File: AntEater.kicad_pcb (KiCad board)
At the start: 2 copper layers, 50.1 x 30.1 mm, 5 parts, among them CN1 X2026WRS-2X09D-LPSW, CN2 X2026WRS-2X09D-LPSW, J1 Conn_01x10_MountingPin

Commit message: placed and routed
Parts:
- removed J1: Conn_01x10_MountingPin, Connector_PinHeader_2.54mm:PinHeader_1x11_P2.54mm_Vertical
- added C1: 0.1uF, Capacitor_SMD:C_0805_2012Metric, F.Cu at (161.4, 77.7)
- added C10: 3.3uF, Capacitor_SMD:C_0805_2012Metric, F.Cu at (161.1, 66.3)
- added C11: 0.1uF, Capacitor_SMD:C_0805_2012Metric, F.Cu at (176.4, 74.0)
- added C12: 0.1uF, Capacitor_SMD:C_0805_2012Metric, F.Cu at (165.3, 79.5)
- added C13: 0.1uF, Capacitor_SMD:C_0805_2012Metric, F.Cu at (161.1, 71.6)
- added C14: 0.1uF, Capacitor_SMD:C_0805_2012Metric, F.Cu at (161.1, 68.3)
- added C2: 27pf, Capacitor_SMD:C_0805_2012Metric, F.Cu at (154.8, 82.9)
- added C3: 0.1uF, Capacitor_SMD:C_0805_2012Metric, F.Cu at (176.0, 78.9)
- added C4: 4.7uF, Capacitor_SMD:C_1206_3216Metric, F.Cu at (164.7, 81.7)
- added C5: 0.1uF, Capacitor_SMD:C_0805_2012Metric, F.Cu at (175.4, 66.1)
- added C6: 4.7uF, Capacitor_SMD:C_1206_3216Metric, F.Cu at (171.4, 81.6)
- added C7: 27pf, Capacitor_SMD:C_0805_2012Metric, F.Cu at (161.1, 82.9)
- added C8: 0.1uF, Capacitor_SMD:C_0805_2012Metric, F.Cu at (177.3, 68.5)
- added C9: 0.1uF, Capacitor_SMD:C_0805_2012Metric, F.Cu at (170.3, 79.4)
- added FB1: FerriteBead_Small, Resistor_SMD:R_0603_1608Metric, F.Cu at (175.4, 81.4)
- added FB2: FerriteBead_Small, Resistor_SMD:R_0603_1608Metric, F.Cu at (175.4, 83.0)
- added J2: USB_C_Receptacle_USB2.0, Connector_USB:USB_C_Receptacle_GCT_USB4105-xx-A_16P_TopMnt_Horizontal, F.Cu at (168.4, 87.6)
- added J3: Conn_02x06_Odd_Even, Connector_PinHeader_2.54mm:PinHeader_2x06_P2.54mm_Vertical, F.Cu at (167.3, 46.2)
- added JP1: SolderJumper_2_Open, Jumper:SolderJumper-2_P1.3mm_Open_RoundedPad1.0x1.5mm, F.Cu at (169.1, 63.7)
- added JP2: SolderJumper_2_Open, Jumper:SolderJumper-2_P1.3mm_Open_RoundedPad1.0x1.5mm, F.Cu at (176.2, 71.4)
- added R1: 2.2K, Resistor_SMD:R_0805_2012Metric, F.Cu at (156.5, 72.0)
- added R2: 10K, Resistor_SMD:R_0805_2012Metric, F.Cu at (158.4, 72.0)
- added R3: 10K, Resistor_SMD:R_0805_2012Metric, F.Cu at (152.7, 72.0)
- added R4: 10K, Resistor_SMD:R_0805_2012Metric, F.Cu at (154.6, 72.0)
- added R5: 5.1K, Resistor_SMD:R_0805_2012Metric, F.Cu at (175.9, 87.9)
- added R6: 12K, Resistor_SMD:R_0805_2012Metric, F.Cu at (154.2, 79.9)
- added R7: 5.1K, Resistor_SMD:R_0805_2012Metric, F.Cu at (161.0, 87.9)
- added R8: 1K, Resistor_SMD:R_0805_2012Metric, F.Cu at (175.9, 77.0)
- added U1: M93C46-WDW6TP, bitcrane:TSSOP8_STM, F.Cu at (155.4, 76.5)
- added U2: FT4232HQ, bitcrane:QFN50P900X900X105-65N, F.Cu at (168.3, 71.7)
- added Y1: 12MHz, bitcrane:XTAL_405C35B12M00000, F.Cu at (158.0, 83.1)
- moved G*** 73.3 mm to (228.9, 26.7)
- moved Ge 66.4 mm to (235.0, 26.9)
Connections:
- net /3V3 renamed VCCIO
- net GND renamed /GND
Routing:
- net /TX: track 25.2 -> 80.4 mm, vias 0 -> 5
- net /GND: track 25.0 -> 76.6 mm, vias 10 -> 39
- net /SDA: track 24.9 -> 75.4 mm, vias 0 -> 2
- net VCORE: track 0.00 -> 45.5 mm, vias 0 -> 4
- net /SCL: track 48.5 -> 89.8 mm, vias 0 -> 2
- net /A0: track 74.9 -> 49.5 mm, vias 0 -> 2
- net Net-(U2-REF): track 0.00 -> 21.3 mm, vias 0 -> 2
- net Net-(U2-VPHY): track 0.00 -> 18.6 mm, vias 0 -> 2
- net VCCIO: track 51.0 -> 33.4 mm, vias 0 -> 13
- net Net-(U1-CS): track 0.00 -> 14.5 mm
- net Net-(U2-OSCI): track 0.00 -> 13.0 mm
- net Net-(U1-CLK): track 0.00 -> 12.8 mm
- net Net-(U2-VPLL): track 0.00 -> 12.5 mm
- net Net-(U2-OSCO): track 0.00 -> 12.1 mm
- net Net-(U1-D): track 0.00 -> 11.1 mm
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- added copper zone on In1.Cu, net /GND
- added copper zone on In2.Cu, net VCCIO
- removed copper zone on B.Cu, net /GND
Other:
- board size 50.1 x 30.1 mm -> 49.8 x 48.6 mm
- copper layers 2 -> 4
- board text removed: "Revision 2"

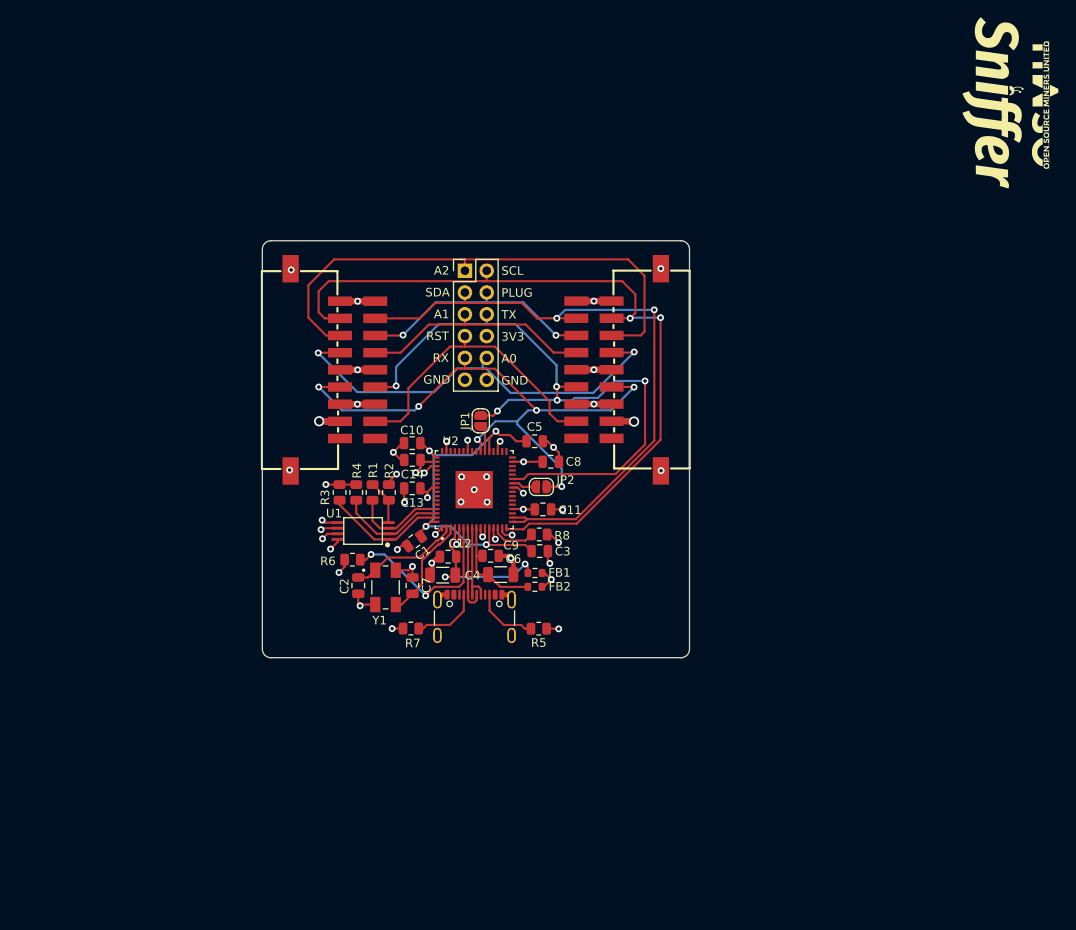
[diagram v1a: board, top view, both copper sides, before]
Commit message: added an optional voltage regulator. DRC passed. generated gerbers
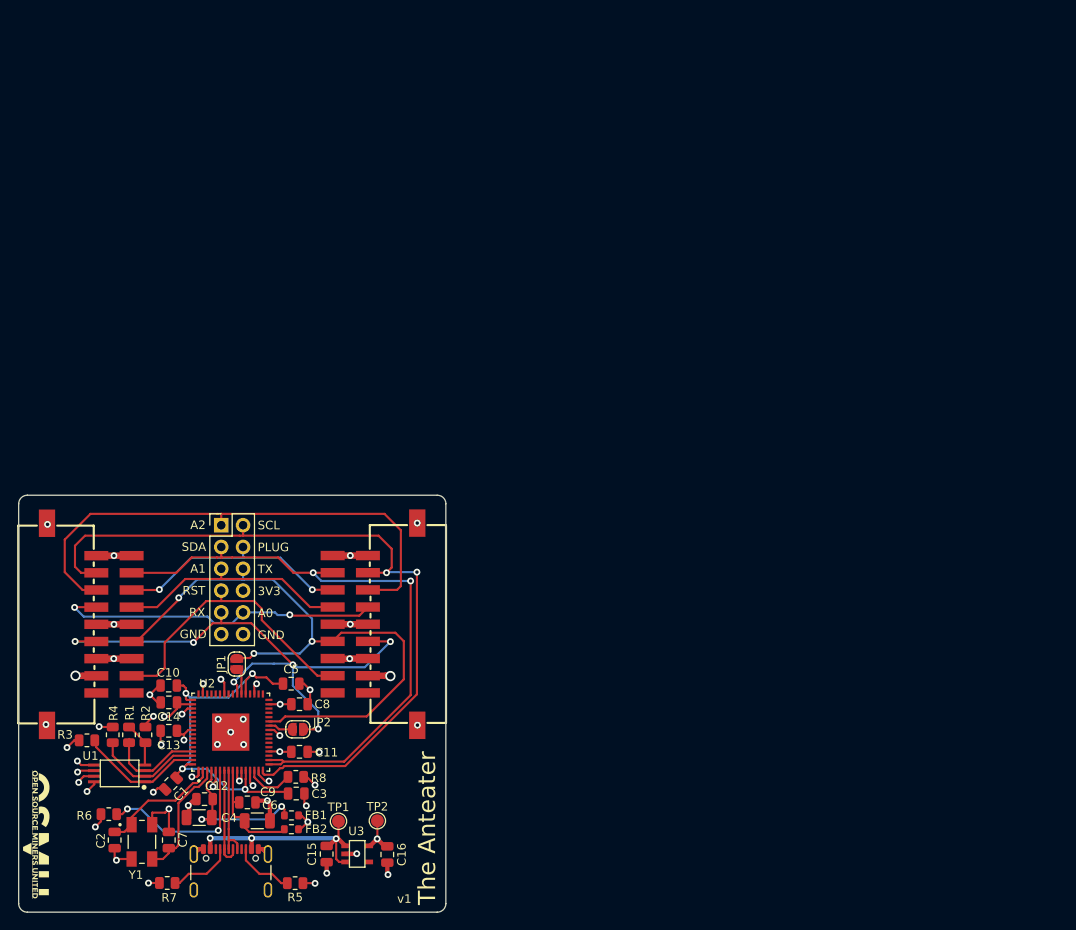
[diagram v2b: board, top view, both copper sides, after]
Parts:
- removed G***: SnifferLOGO, antsniffer:SnifferLOGO
- added C15: 1uF, Capacitor_SMD:C_0805_2012Metric, F.Cu at (151.2, 114.2)
- added C16: 1uF, Capacitor_SMD:C_0805_2012Metric, F.Cu at (158.2, 114.2)
- added TP1: TestPoint, TestPoint:TestPoint_Pad_D1.5mm, F.Cu at (152.5, 110.4)
- added TP2: TestPoint, TestPoint:TestPoint_Pad_D1.5mm, F.Cu at (157.1, 110.3)
- added U3: RT9080-33GJ5, antsniffer:RT9080-33GJ5, F.Cu at (154.7, 114.2)
- J2: footprint Connector_USB:USB_C_Receptacle_GCT_USB4105-xx-A_16P_TopMnt_Horizontal -> antsniffer:USB_C_Receptacle_GCT_USB4105-xx-A_16P_TopMnt_Horizontal
- moved Ge 145.3 mm to (117.2, 111.9), turned to -90 degrees
- moved R3 41.2 mm to (123.2, 100.9), turned to 180 degrees
- moved C7 41.1 mm to (132.8, 112.6)
- moved CN1 41.1 mm to (123.5, 87.4)
- moved R7 41.1 mm to (132.6, 117.6)
- moved C2 41.1 mm to (126.4, 112.6)
- moved CN2 41.1 mm to (156.8, 87.4)
- moved R5 41.1 mm to (147.5, 117.6)
- moved R6 41.1 mm to (125.8, 109.5)
- moved J3 41.1 mm to (138.9, 75.9)
- moved Y1 41.1 mm to (129.6, 112.8)
- moved J2 41.0 mm to (140.0, 117.3)
- moved C8 40.7 mm to (148.0, 96.7)
- moved C9 40.4 mm to (141.9, 108.2)
- moved C6 40.3 mm to (143.1, 110.3)
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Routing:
- net /5V: track 0.00 -> 25.9 mm, vias 0 -> 3
- net /A0: track 49.5 -> 38.6 mm
- net /GND: track 76.6 -> 84.7 mm, vias 39 -> 42
- net /TX: track 80.4 -> 73.2 mm, vias 5 -> 3
- net VCCIO: track 33.4 -> 38.5 mm, vias 13 -> 15
- net /RX: track 70.8 -> 67.3 mm
- net /SDA: track 75.4 -> 72.8 mm
- net Net-(U2-OSCO): track 12.1 -> 14.5 mm
- net Net-(U2-DP): track 9.58 -> 11.0 mm
- net Net-(U2-DM): track 10.3 -> 11.7 mm
- net Net-(U2-OSCI): track 13.0 -> 14.2 mm
- net Net-(U2-VPLL): track 12.5 -> 13.5 mm
- net Net-(U2-REF): track 21.3 -> 20.3 mm
- net VCORE: track 45.5 -> 46.4 mm
- net Net-(U2-RESET#): track 5.21 -> 5.72 mm
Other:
- board text added: "The Anteater"
- board text added: "v1"
- board text removed: "The AntSniffer"
- board text removed: "by OSMU"
